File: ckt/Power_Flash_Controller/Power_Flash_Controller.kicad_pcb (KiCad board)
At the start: 2 copper layers, 84.5 x 67.5 mm, 30 parts, among them J2 Screw_Terminal_01x03, J3 Screw_Terminal_01x03, J4 Screw_Terminal_01x03, K4 SANYOU_SRD_Form_C, K5 SANYOU_SRD_Form_C, K6 SANYOU_SRD_Form_C, Q1 BC857, Q2 BC857, Q3 BC857, U1 PC817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

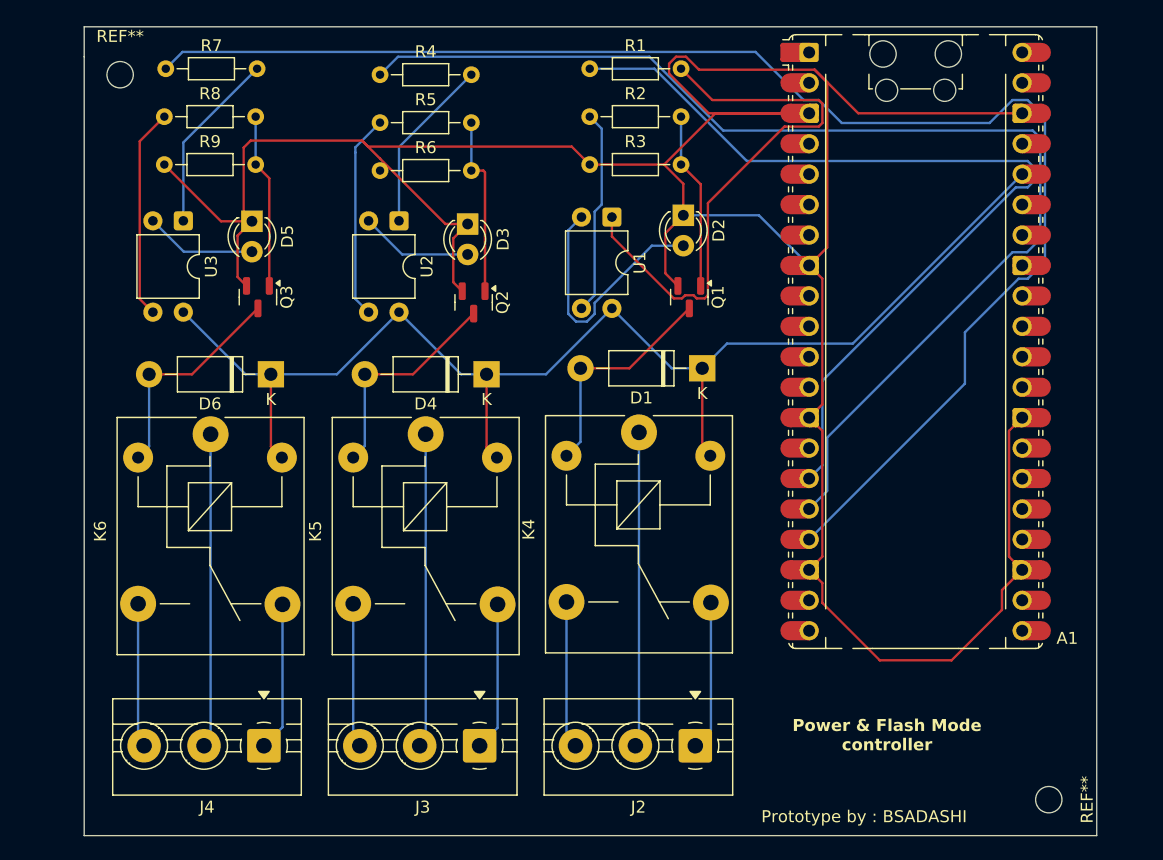
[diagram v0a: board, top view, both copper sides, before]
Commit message: Added 2.1mm Screw holes for mounting and added divet in PCB for microusb port
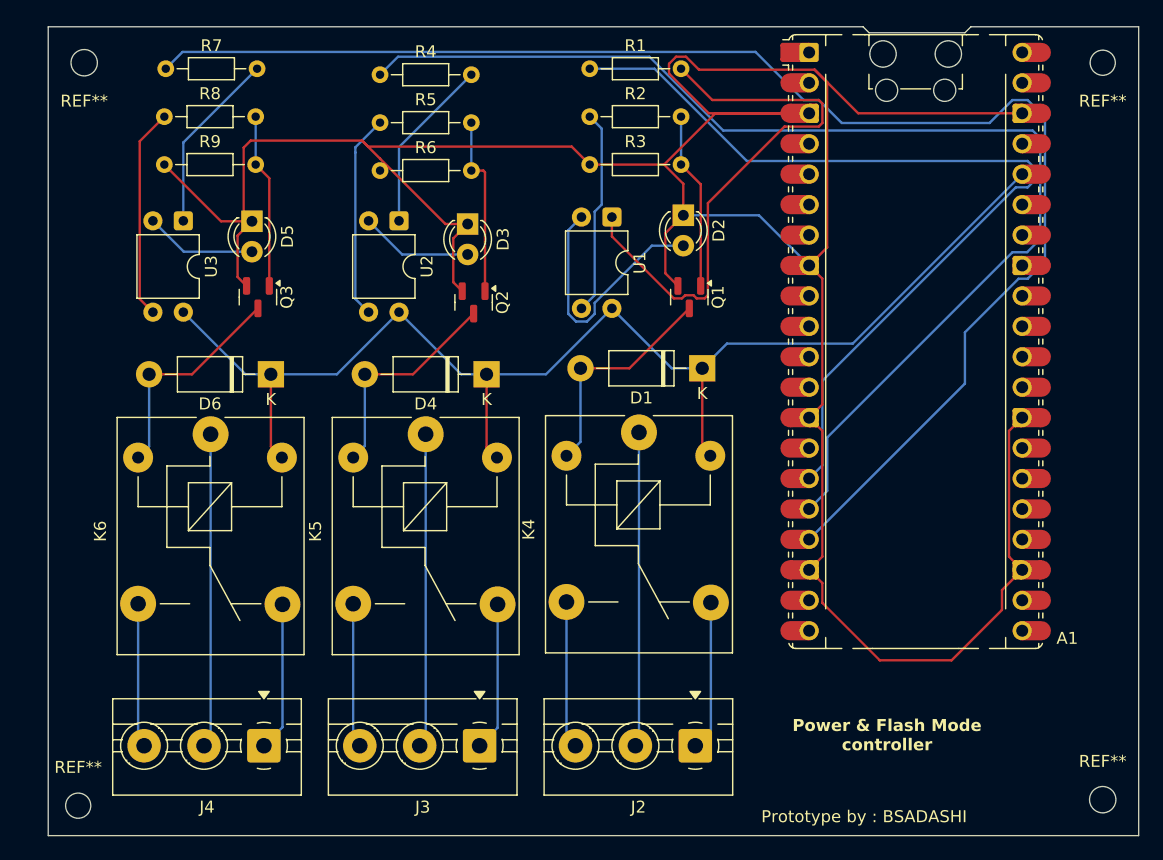
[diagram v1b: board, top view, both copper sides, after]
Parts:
- added REF**: MountingHole_2.1mm, MountingHole:MountingHole_2.1mm, F.Cu at (187.5, 71.5)
- added REF**: MountingHole_2.1mm, MountingHole:MountingHole_2.1mm, F.Cu at (102.0, 133.5)
- moved REF** 4.50 mm to (187.5, 133.0), turned to 0 degrees
- moved REF** 3.16 mm to (102.5, 71.5), turned to 180 degrees
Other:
- board size 84.5 x 67.5 mm -> 91 x 67.5 mm

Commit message: Added M2 holes for mounting and updated board design
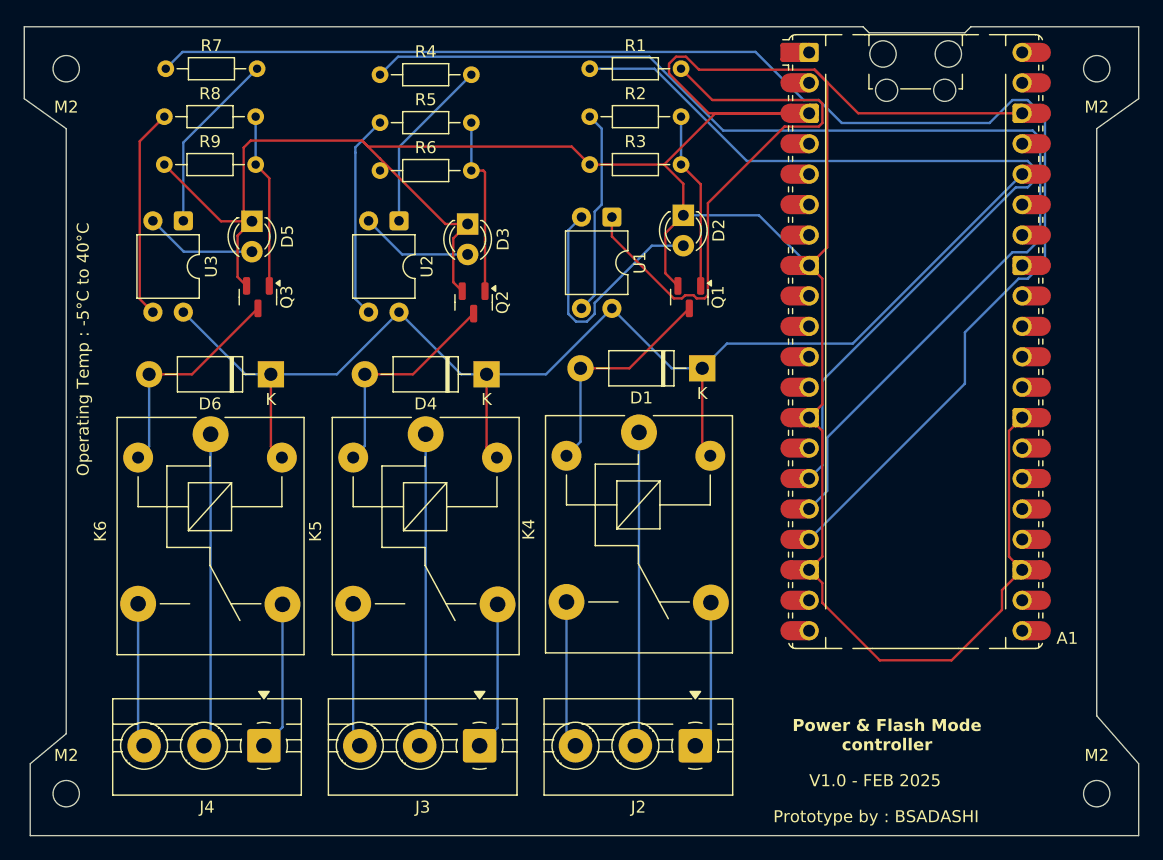
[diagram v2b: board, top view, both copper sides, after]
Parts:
- removed REF** (x2): MountingHole_2.2mm_M2, MountingHole:MountingHole_2.2mm_M2
- removed REF** (x2): MountingHole_2.1mm, MountingHole:MountingHole_2.1mm
- added M2: MountingHole_2.2mm_M2, MountingHole:MountingHole_2.2mm_M2, F.Cu at (101.0, 72.0)
- added M2: MountingHole_2.2mm_M2, MountingHole:MountingHole_2.2mm_M2, F.Cu at (101.0, 132.5)
- added M2: MountingHole_2.2mm_M2, MountingHole:MountingHole_2.2mm_M2, F.Cu at (187.0, 132.5)
- added M2: MountingHole_2.2mm_M2, MountingHole:MountingHole_2.2mm_M2, F.Cu at (187.0, 72.0)
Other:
- board size 91 x 67.5 mm -> 93 x 67.5 mm
- board text added: "MAX 12V DC"
- board text added: "Operating Temp : -5°C to 40°C"
- board text added: "V1.0 - FEB 2025"
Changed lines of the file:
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@@
 	(footprint "MountingHole:MountingHole_2.2mm_M2"
 		(layer "F.Cu")
-		(at 102.5 71.5 180)
+		(at 101 72 180)
 		(descr "Mounting Hole 2.2mm, no annular, M2")
 		(tags "mounting hole 2.2mm no annular m2")
-		(property "Reference" "REF**"
+		(property "Reference" "M2"
 			(at 0 -3.2 0)
 			(layer "F.SilkS")
@@
 	(footprint "MountingHole:MountingHole_2.2mm_M2"
 		(layer "F.Cu")
-		(at 187.5 133)
+		(at 101 132.5)
 		(descr "Mounting Hole 2.2mm, no annular, M2")
 		(tags "mounting hole 2.2mm no annular m2")
-		(property "Reference" "REF**"
+		(property "Reference" "M2"
 			(at 0 -3.2 0)
 			(layer "F.SilkS")
@@
 		)
 	)
-	(footprint "MountingHole:MountingHole_2.1mm"
-		(layer "F.Cu")
-		(at 187.5 71.5 180)
-		(descr "Mounting Hole 2.1mm, no annular")
-		(tags "mounting hole 2.1mm no annular")
-		(property "Reference" "REF**"
-			(at 0 -3.2 0)
-			(layer "F.SilkS")
-			(effects
-				(font
-					(size 1 1)
-					(thickness 0.15)
-				)
-			)
-		)
-		(property "Value" "MountingHole_2.1mm"
-			(at 0 3.2 0)
-			(layer "F.Fab")
-			(effects
-				(font
-					(size 1 1)
-					(thickness 0.15)
-				)
-			)
-		)
-		(property "Datasheet" ""
-			(at 0 0 180)
-			(unlocked yes)
-			(layer "F.Fab")
-			(hide yes)
-			(effects
-				(font
-					(size 1.27 1.27)
-					(thickness 0.15)
-				)
-			)
-		)
-		(property "Description" ""
-			(at 0 0 180)
-			(unlocked yes)
-			(layer "F.Fab")
-			(hide yes)
-			(effects
-				(font
-					(size 1.27 1.27)
-					(thickness 0.15)
-				)
-			)
-		)
-		(attr exclude_from_pos_files exclude_from_bom)
-		(fp_circle
-			(center 0 0)
-			(end 2.1 0)
-			(stroke
-				(width 0.15)
-				(type solid)
-			)
-			(fill no)
-			(layer "Cmts.User")
-		)
-		(fp_circle
-			(center 0 0)
-			(end 2.35 0)
-			(stroke
-				(width 0.05)
-				(type solid)
-			)
-			(fill no)
-			(layer "F.CrtYd")
-		)
-		(fp_text user "${REFERENCE}"
-			(at 0 0 0)
-			(layer "F.Fab")
-			(effects
-				(font
-					(size 1 1)
-					(thickness 0.15)
-				)
-			)
-		)
-		(pad "" np_thru_hole circle
-			(at 0 0 180)
-			(size 2.1 2.1)
-			(drill 2.1)
-			(layers "*.Cu" "*.Mask")
-		)
-		(embedded_fonts no)
-	)
 	(footprint "Package_TO_SOT_SMD:SOT-23"
 		(placed yes)
@@
 		)
 	)
-	(footprint "MountingHole:MountingHole_2.1mm"
+	(footprint "MountingHole:MountingHole_2.2mm_M2"
 		(layer "F.Cu")
-		(at 102 133.5)
-		(descr "Mounting Hole 2.1mm, no annular")
-		(tags "mounting hole 2.1mm no annular")
-		(property "Reference" "REF**"
+		(at 187 132.5)
+		(descr "Mounting Hole 2.2mm, no annular, M2")
+		(tags "mounting hole 2.2mm no annular m2")
+		(property "Reference" "M2"
 			(at 0 -3.2 0)
 			(layer "F.SilkS")
@@
 			)
 		)
-		(property "Value" "MountingHole_2.1mm"
+		(property "Value" "MountingHole_2.2mm_M2"
 			(at 0 3.2 0)
 			(layer "F.Fab")
@@
 		(fp_circle
 			(center 0 0)
-			(end 2.1 0)
+			(end 2.2 0)
 			(stroke
 				(width 0.15)
@@
 		(fp_circle
 			(center 0 0)
-			(end 2.35 0)
+			(end 2.45 0)
 			(stroke
 				(width 0.05)
@@
 		(pad "" np_thru_hole circle
 			(at 0 0)
-			(size 2.1 2.1)
-			(drill 2.1)
+			(size 2.2 2.2)
+			(drill 2.2)
 			(layers "*.Cu" "*.Mask")
 		)
@@
 		)
 	)
+	(footprint "MountingHole:MountingHole_2.2mm_M2"
+		(layer "F.Cu")
+		(at 187 72 180)
+		(descr "Mounting Hole 2.2mm, no annular, M2")
+		(tags "mounting hole 2.2mm no annular m2")
+		(property "Reference" "M2"
+			(at 0 -3.2 0)
+			(layer "F.SilkS")
+			(effects
+				(font
+					(size 1 1)
+					(thickness 0.15)
+				)
+			)
+		)
+		(property "Value" "MountingHole_2.2mm_M2"
+			(at 0 3.2 0)
+			(layer "F.Fab")
+			(effects
+				(font
+					(size 1 1)
+					(thickness 0.15)
+				)
+			)
+		)
+		(property "Datasheet" ""
+			(at 0 0 180)
+			(unlocked yes)
+			(layer "F.Fab")
+			(hide yes)
+			(effects
+				(font
+					(size 1.27 1.27)
+					(thickness 0.15)
+				)
+			)
+		)
+		(property "Description" ""
+			(at 0 0 180)
+			(unlocked yes)
+			(layer "F.Fab")
+			(hide yes)
+			(effects
+				(font
+					(size 1.27 1.27)
+					(thickness 0.15)
+				)
+			)
+		)
+		(attr exclude_from_pos_files exclude_from_bom)
+		(fp_circle
+			(center 0 0)
+			(end 2.2 0)
+			(stroke
+				(width 0.15)
+				(type solid)
+			)
+			(fill no)
+			(layer "Cmts.User")
+		)
+		(fp_circle
+			(center 0 0)
+			(end 2.45 0)
+			(stroke
+				(width 0.05)
+				(type solid)
+			)
+			(fill no)
+			(layer "F.CrtYd")
+		)
+		(fp_text user "${REFERENCE}"
+			(at 0 0 0)
+			(layer "F.Fab")
+			(effects
+				(font
+					(size 1 1)
+					(thickness 0.15)
+				)
+			)
+		)
+		(pad "" np_thru_hole circle
+			(at 0 0 180)
+			(size 2.2 2.2)
+			(drill 2.2)
+			(layers "*.Cu" "*.Mask")
+		)
+		(embedded_fonts no)
+	)
 	(footprint "Resistor_THT:R_Axial_DIN0204_L3.6mm_D1.6mm_P7.62mm_Horizontal"
 		(placed yes)
@@
 	)
 	(gr_line
-		(start 190.5 136)
-		(end 190.5 68.5)
+		(start 187 126)
+		(end 187 77)
 		(stroke
 			(width 0.05)
@@
 	)
 	(gr_line
-		(start 99.5 136)
+		(start 98 136)
 		(end 190.5 136)
 		(stroke
@@
 	)
 	(gr_line
+		(start 98 136)
+		(end 98 130)
+		(stroke
+			(width 0.05)
+			(type default)
+		)
+		(layer "Edge.Cuts")
+	)
+	(gr_line
 		(start 167.5 68.5)
-		(end 99.5 68.5)
+		(end 97.5 68.5)
+		(stroke
+			(width 0.05)
+			(type default)
+		)
+		(layer "Edge.Cuts")
+	)
+	(gr_line
+		(start 190.5 130)
+		(end 187 126)
 		(stroke
 			(width 0.05)
@@
 	)
 	(gr_line
+		(start 97.5 74.5)
+		(end 97.5 68.5)
+		(stroke
+			(width 0.05)
+			(type default)
+		)
+		(layer "Edge.Cuts")
+	)
+	(gr_line
+		(start 98 130)
+		(end 101 127.5)
+		(stroke
+			(width 0.05)
+			(type default)
+		)
+		(layer "Edge.Cuts")
+	)
+	(gr_line
+		(start 187 77)
+		(end 190.5 74.5)
+		(stroke
+			(width 0.05)
+			(type default)
+		)
+		(layer "Edge.Cuts")
+	)
+	(gr_line
 		(start 190.5 68.5)
 		(end 176.5 68.5)
@@
 	)
 	(gr_line
+		(start 190.5 74.5)
+		(end 190.5 68.5)
+		(stroke
+			(width 0.05)
+			(type default)
+		)
+		(layer "Edge.Cuts")
+	)
+	(gr_line
+		(start 190.5 136)
+		(end 190.5 130)
+		(stroke
+			(width 0.05)
+			(type default)
+		)
+		(layer "Edge.Cuts")
+	)
+	(gr_line
 		(start 176.5 68.5)
 		(end 176 69)
@@
 	)
 	(gr_line
-		(start 99.5 68.5)
-		(end 99.5 136)
+		(start 101 127.5)
+		(end 101 77)
+		(stroke
+			(width 0.05)
+			(type default)
+		)
+		(layer "Edge.Cuts")
+	)
+	(gr_line
+		(start 101 77)
+		(end 97.5 74.5)
 		(stroke
 			(width 0.05)
@@
 		(layer "Edge.Cuts")
 	)
+	(gr_text "V1.0 - FEB 2025"
+		(at 163 132 0)
+		(layer "F.SilkS")
+		(effects
+			(font
+				(size 1 1)
+				(thickness 0.15)
+			)
+			(justify left bottom)
+		)
+	)
 	(gr_text "Power & Flash Mode \ncontroller"
 		(at 169.5 129 0)
@@
 		)
 	)
+	(gr_text "Operating Temp : -5°C to 40°C"
+		(at 103 106 90)
+		(layer "F.SilkS")
+		(effects
+			(font
+				(size 1 1)
+				(thickness 0.15)
+			)
+			(justify left bottom)
+		)
+	)
 	(gr_text "Prototype by : BSADASHI"
-		(at 159 135 0)
+		(at 160 135 0)
 		(layer "F.SilkS")
 		(effects
@@
 			)
 			(justify left bottom)
+		)
+	)
+	(gr_text "MAX 12V DC\n"
+		(at 126.5 135.5 0)
+		(layer "Edge.Cuts")
+		(effects
+			(font
+				(size 1 1)
+				(thickness 0.15)
+			)
+			(justify left bottom)
